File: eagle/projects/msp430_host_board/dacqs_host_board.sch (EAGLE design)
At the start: 107 parts, among them J1 MOL-SL-4-RA, J10 MOL-SL-3-V, J12 MOL-SL-2-V, J13 JST-PH-2TH-RA, J14 USB_MICROB_RECPT, J16 MOL-SL-2-RA, J17 CLM-112-02-L-D, J2 MOL-SL-4-RA, J3 MOL-SL-4-RA, J4 MOL-SL-4-RA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

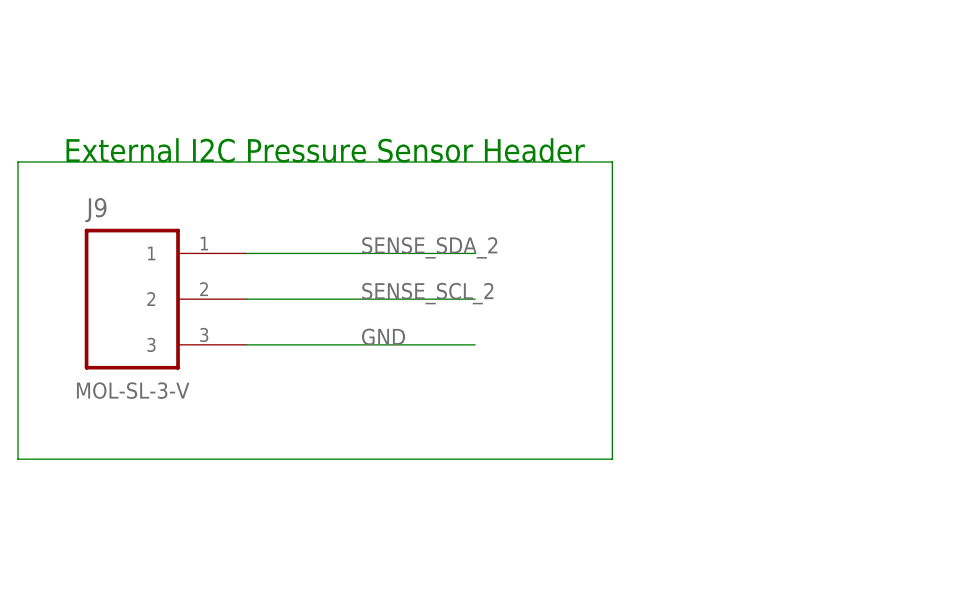
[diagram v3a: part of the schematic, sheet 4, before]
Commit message: Added power to balloon pressure sensor connector
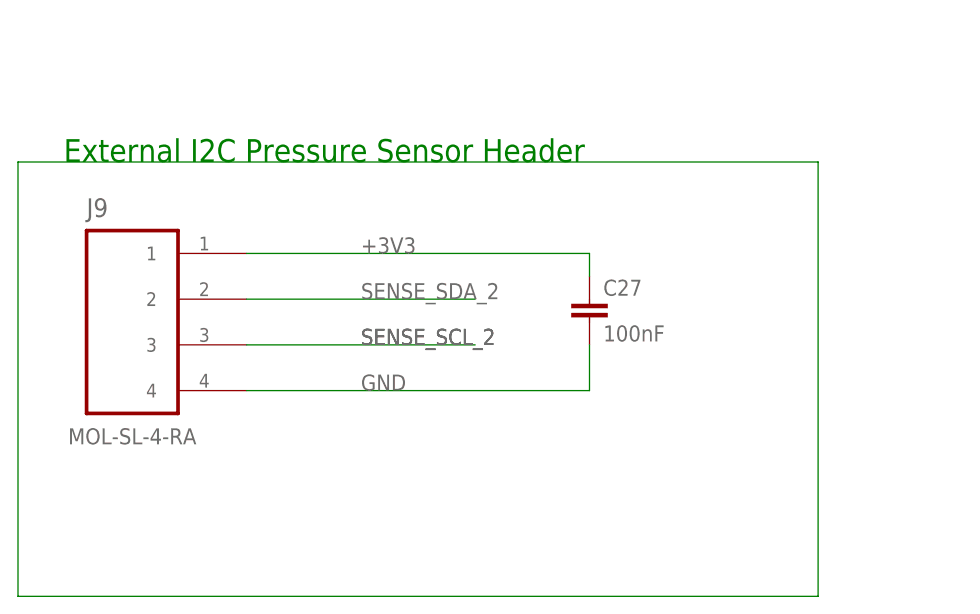
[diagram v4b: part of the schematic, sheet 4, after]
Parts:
- added C27: 100nF, daqcs_host:CAP_100NF0_0603
- J9: value MOL-SL-3-V -> MOL-SL-4-RA; device daqcs_host:MOLSL_3PIN_SL3V_V -> daqcs_host:MOLSL_4PIN_SL4RA_RA
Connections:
- net +3V3: now also C27.1, J9.1
- net GND: now also C27.2, J9.4; no longer J9.3
- net SENSE_SCL_2: now also J9.3; no longer J9.2
- net SENSE_SDA_2: now also J9.2; no longer J9.1
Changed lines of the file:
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@@
 <setting verticaltext="up"/>
 </settings>
-<grid distance="0.1" unitdist="inch" unit="inch" style="lines" multiple="1" display="yes" altdistance="0.01" altunitdist="inch" altunit="inch"/>
+<grid distance="0.1" unitdist="inch" unit="inch" style="lines" multiple="1" display="no" altdistance="0.01" altunitdist="inch" altunit="inch"/>
 <layers>
 <layer number="1" name="Top" color="4" fill="1" visible="no" active="no"/>
@@
 <part name="J7" library="daqcs_host" deviceset="MOLSL_5PIN" device="_V" technology="_SL4V" value="MOL-SL-5-V"/>
 <part name="J8" library="daqcs_host" deviceset="MOLSL_3PIN" device="_RA" technology="_SL3RA" value="MOL-SL-3-RA"/>
-<part name="J9" library="daqcs_host" deviceset="MOLSL_3PIN" device="_V" technology="_SL3V" value="MOL-SL-3-V"/>
 <part name="J10" library="daqcs_host" deviceset="MOLSL_3PIN" device="_V" technology="_SL3V" value="MOL-SL-3-V"/>
 <part name="H1" library="daqcs_host" deviceset="MOUNT-HOLE" device="_2.75"/>
@@
 <part name="SUPPLY36" library="supply2" deviceset="GND" device=""/>
 <part name="SUPPLY37" library="supply2" deviceset="GND" device=""/>
+<part name="J9" library="daqcs_host" deviceset="MOLSL_4PIN" device="_RA" technology="_SL4RA" value="MOL-SL-4-RA"/>
+<part name="C27" library="daqcs_host" deviceset="CAP" device="_0603" technology="_100NF0" value="100nF"/>
 </parts>
 <sheets>
@@
 <instance part="J7" gate="G$1" x="55.88" y="195.58"/>
 <instance part="J8" gate="G$1" x="55.88" y="134.62"/>
-<instance part="J9" gate="G$1" x="55.88" y="66.04"/>
 <instance part="J10" gate="G$1" x="218.44" y="127"/>
 <instance part="H1" gate="G$1" x="213.36" y="71.12"/>
@@
 <instance part="H3" gate="G$1" x="213.36" y="55.88"/>
 <instance part="H4" gate="G$1" x="256.54" y="55.88"/>
+<instance part="J9" gate="G$1" x="55.88" y="63.5"/>
+<instance part="C27" gate="G$1" x="106.68" y="63.5"/>
 </instances>
 <busses>
@@
 </segment>
 <segment>
-<wire x1="68.58" y1="60.96" x2="93.98" y2="60.96" width="0.1524" layer="91"/>
-<label x="81.28" y="60.96" size="1.778" layer="95"/>
-<pinref part="J9" gate="G$1" pin="3"/>
-</segment>
-<segment>
 <pinref part="SUPPLY10" gate="GND" pin="GND"/>
 <wire x1="195.58" y1="182.88" x2="195.58" y2="187.96" width="0.1524" layer="91"/>
@@
 <pinref part="J10" gate="G$1" pin="3"/>
 </segment>
+<segment>
+<pinref part="J9" gate="G$1" pin="4"/>
+<wire x1="68.58" y1="55.88" x2="106.68" y2="55.88" width="0.1524" layer="91"/>
+<label x="81.28" y="55.88" size="1.778" layer="95"/>
+<pinref part="C27" gate="G$1" pin="2"/>
+<wire x1="106.68" y1="60.96" x2="106.68" y2="55.88" width="0.1524" layer="91"/>
+</segment>
 </net>
 <net name="ACT_SPEED_IN" class="0">
@@
 <net name="SENSE_SDA_2" class="0">
 <segment>
-<wire x1="68.58" y1="71.12" x2="93.98" y2="71.12" width="0.1524" layer="91"/>
-<label x="81.28" y="71.12" size="1.778" layer="95"/>
-<pinref part="J9" gate="G$1" pin="1"/>
-</segment>
-</net>
-<net name="SENSE_SCL_2" class="0">
-<segment>
 <wire x1="68.58" y1="66.04" x2="93.98" y2="66.04" width="0.1524" layer="91"/>
 <label x="81.28" y="66.04" size="1.778" layer="95"/>
 <pinref part="J9" gate="G$1" pin="2"/>
+</segment>
+</net>
+<net name="SENSE_SCL_2" class="0">
+<segment>
+<wire x1="68.58" y1="60.96" x2="93.98" y2="60.96" width="0.1524" layer="91"/>
+<label x="81.28" y="60.96" size="1.778" layer="95"/>
+<pinref part="J9" gate="G$1" pin="3"/>
+<label x="81.28" y="60.96" size="1.778" layer="95"/>
 </segment>
 </net>
@@
 <wire x1="246.38" y1="203.2" x2="246.38" y2="208.28" width="0.1524" layer="91"/>
 </segment>
+<segment>
+<wire x1="68.58" y1="71.12" x2="106.68" y2="71.12" width="0.1524" layer="91"/>
+<label x="81.28" y="71.12" size="1.778" layer="95"/>
+<pinref part="J9" gate="G$1" pin="1"/>
+<pinref part="C27" gate="G$1" pin="1"/>
+<wire x1="106.68" y1="71.12" x2="106.68" y2="68.58" width="0.1524" layer="91"/>
+</segment>
 </net>
 <net name="SBWTCK_MOTOR" class="0">
@@
 <net name="N$18" class="0">
 <segment>
-<wire x1="43.18" y1="81.28" x2="109.22" y2="81.28" width="0.1524" layer="91"/>
-<wire x1="109.22" y1="81.28" x2="109.22" y2="48.26" width="0.1524" layer="91"/>
-<wire x1="109.22" y1="48.26" x2="43.18" y2="48.26" width="0.1524" layer="91"/>
-<wire x1="43.18" y1="48.26" x2="43.18" y2="81.28" width="0.1524" layer="91"/>
-</segment>
-</net>
+<wire x1="43.18" y1="81.28" x2="132.08" y2="81.28" width="0.1524" layer="91"/>
+<wire x1="132.08" y1="81.28" x2="132.08" y2="33.02" width="0.1524" layer="91"/>
+<wire x1="132.08" y1="33.02" x2="43.18" y2="33.02" width="0.1524" layer="91"/>
+<wire x1="43.18" y1="33.02" x2="43.18" y2="81.28" width="0.1524" layer="91"/>
+</segment>
+</net>

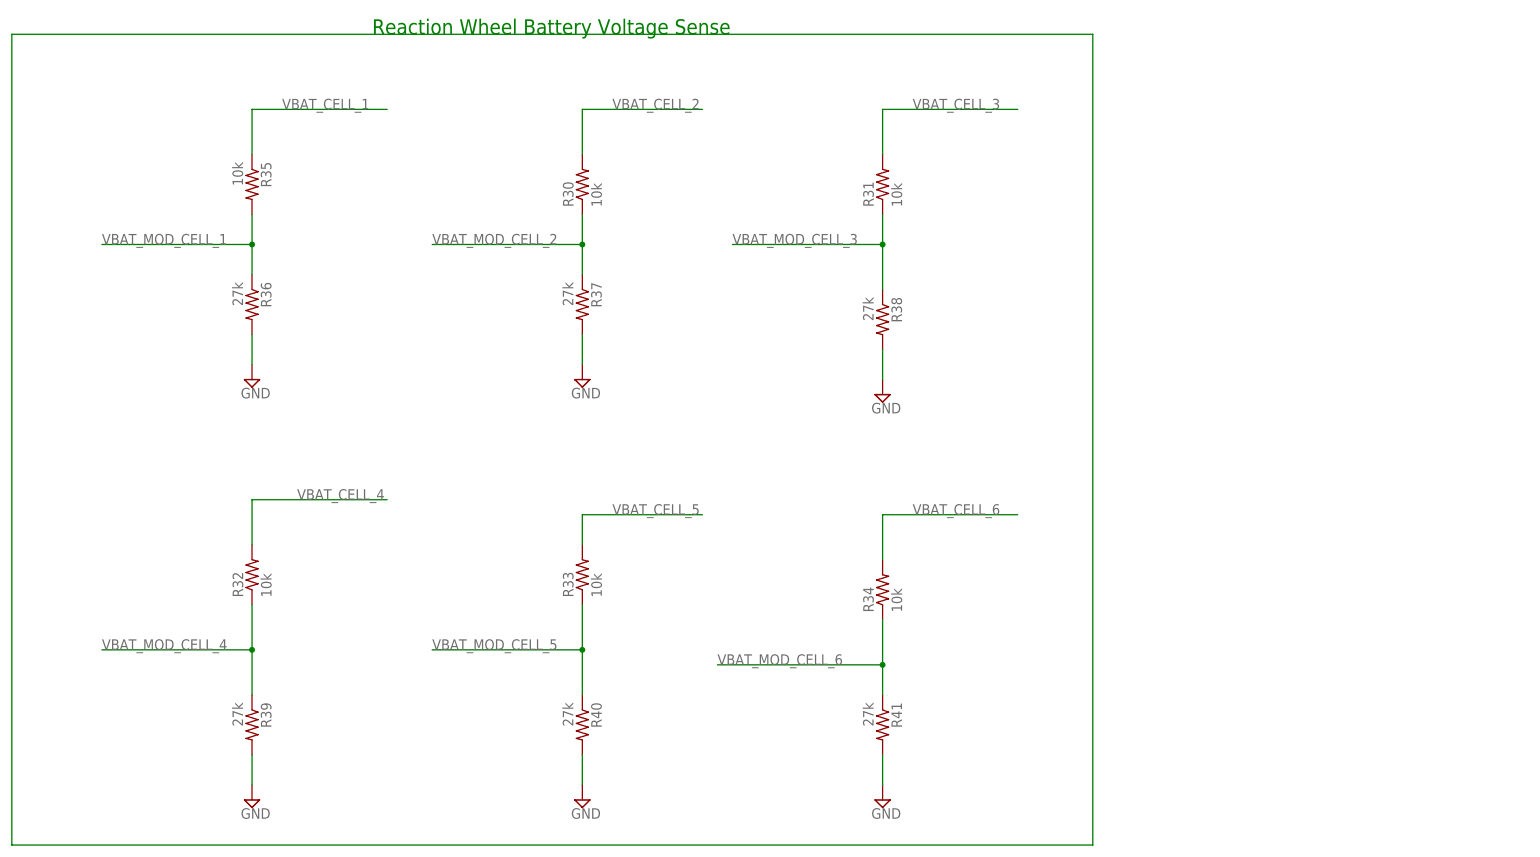
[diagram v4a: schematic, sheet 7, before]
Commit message: Added 7 pin SL connector for reaction wheel battery Vsense
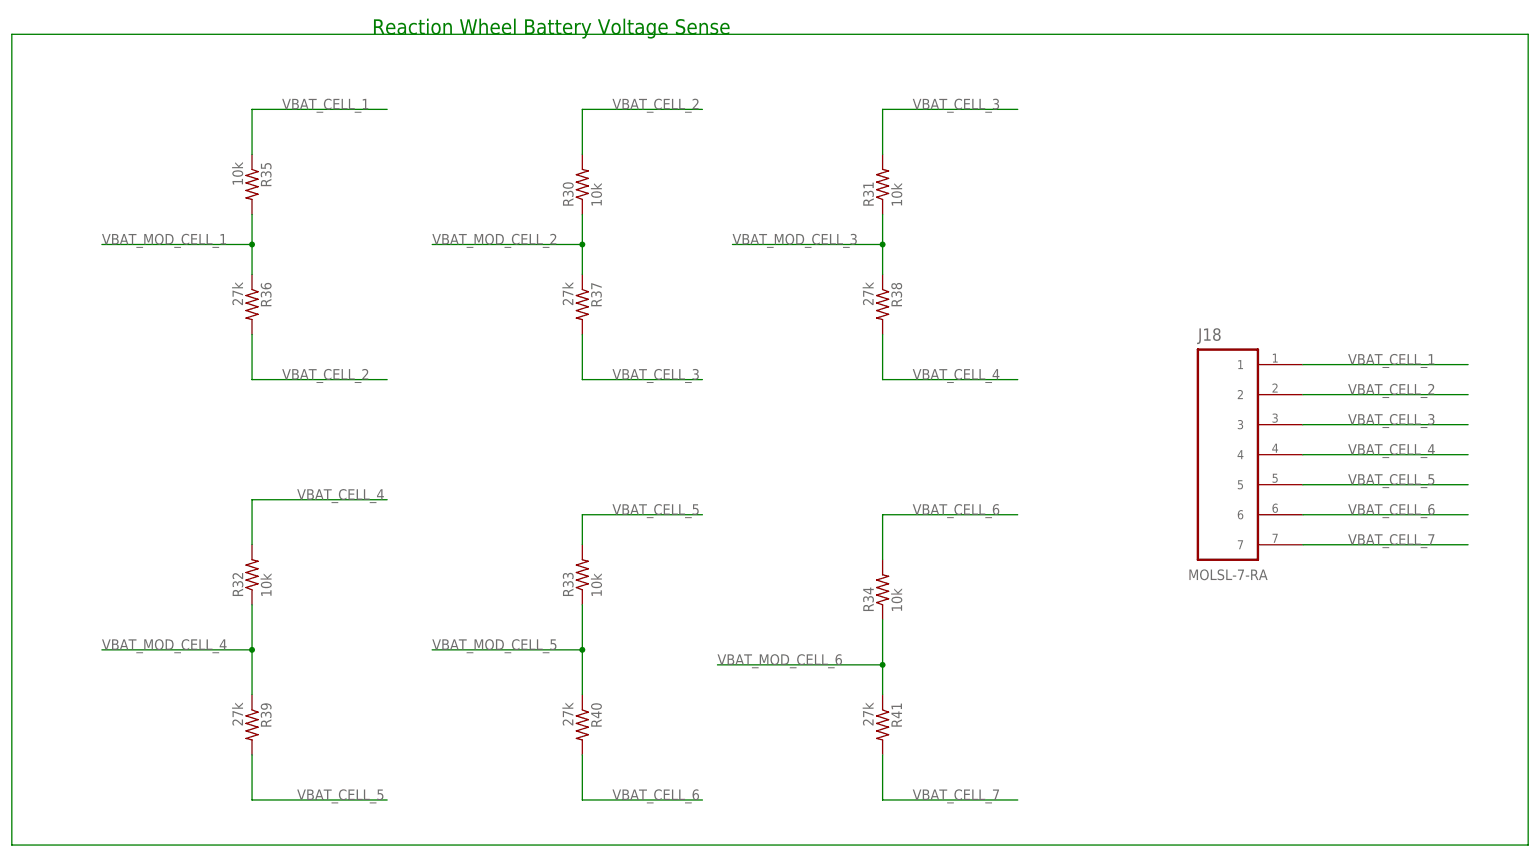
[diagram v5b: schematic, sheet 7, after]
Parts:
- added J18: MOLSL-7-RA, daqcs_host:MOLSL_7PIN_RA
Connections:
- new net VBAT_CELL_7: J18.7, R41.2
- net GND: no longer R36.2, R37.2, R38.2, R39.2, R40.2, R41.2
- net VBAT_CELL_1: now also J18.1
- net VBAT_CELL_2: now also J18.2, R36.2
- net VBAT_CELL_3: now also J18.3, R37.2
- net VBAT_CELL_4: now also J18.4, R38.2
- net VBAT_CELL_5: now also J18.5, R39.2
- net VBAT_CELL_6: now also J18.6, R40.2
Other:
- moved on the sheet: R38
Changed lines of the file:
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@@
 <setting verticaltext="up"/>
 </settings>
-<grid distance="0.1" unitdist="inch" unit="inch" style="lines" multiple="1" display="no" altdistance="0.01" altunitdist="inch" altunit="inch"/>
+<grid distance="0.1" unitdist="inch" unit="inch" style="lines" multiple="1" display="yes" altdistance="0.01" altunitdist="inch" altunit="inch"/>
 <layers>
 <layer number="1" name="Top" color="4" fill="1" visible="no" active="no"/>
@@
 <part name="R40" library="daqcs_host" deviceset="RES" device="_0603" technology="_27R0" value="27k"/>
 <part name="R41" library="daqcs_host" deviceset="RES" device="_0603" technology="_27R0" value="27k"/>
-<part name="SUPPLY31" library="supply2" deviceset="GND" device=""/>
-<part name="SUPPLY33" library="supply2" deviceset="GND" device=""/>
-<part name="SUPPLY34" library="supply2" deviceset="GND" device=""/>
-<part name="SUPPLY35" library="supply2" deviceset="GND" device=""/>
-<part name="SUPPLY36" library="supply2" deviceset="GND" device=""/>
-<part name="SUPPLY37" library="supply2" deviceset="GND" device=""/>
 <part name="J9" library="daqcs_host" deviceset="MOLSL_4PIN" device="_RA" technology="_SL4RA" value="MOL-SL-4-RA"/>
 <part name="C27" library="daqcs_host" deviceset="CAP" device="_0603" technology="_100NF0" value="100nF"/>
+<part name="J18" library="daqcs_host" deviceset="MOLSL_7PIN" device="_RA" value="MOLSL-7-RA"/>
 </parts>
 <sheets>
@@
 <instance part="R36" gate="G$1" x="76.2" y="167.64" rot="R270"/>
 <instance part="R37" gate="G$1" x="132.08" y="167.64" rot="R270"/>
-<instance part="R38" gate="G$1" x="182.88" y="165.1" rot="R270"/>
+<instance part="R38" gate="G$1" x="182.88" y="167.64" rot="R270"/>
 <instance part="R39" gate="G$1" x="76.2" y="96.52" rot="R270"/>
 <instance part="R40" gate="G$1" x="132.08" y="96.52" rot="R270"/>
 <instance part="R41" gate="G$1" x="182.88" y="96.52" rot="R270"/>
-<instance part="SUPPLY31" gate="GND" x="76.2" y="154.94"/>
-<instance part="SUPPLY33" gate="GND" x="132.08" y="154.94"/>
-<instance part="SUPPLY34" gate="GND" x="182.88" y="152.4"/>
-<instance part="SUPPLY35" gate="GND" x="182.88" y="83.82"/>
-<instance part="SUPPLY36" gate="GND" x="132.08" y="83.82"/>
-<instance part="SUPPLY37" gate="GND" x="76.2" y="83.82"/>
+<instance part="J18" gate="G$1" x="241.3" y="142.24"/>
 </instances>
 <busses>
@@
 <wire x1="76.2" y1="200.66" x2="99.06" y2="200.66" width="0.1524" layer="91"/>
 <label x="81.28" y="200.66" size="1.778" layer="95"/>
+</segment>
+<segment>
+<pinref part="J18" gate="G$1" pin="1"/>
+<wire x1="254" y1="157.48" x2="281.94" y2="157.48" width="0.1524" layer="91"/>
+<label x="261.62" y="157.48" size="1.778" layer="95"/>
 </segment>
 </net>
@@
 <label x="137.16" y="200.66" size="1.778" layer="95"/>
 </segment>
+<segment>
+<pinref part="J18" gate="G$1" pin="2"/>
+<wire x1="254" y1="152.4" x2="281.94" y2="152.4" width="0.1524" layer="91"/>
+<label x="261.62" y="152.4" size="1.778" layer="95"/>
+</segment>
+<segment>
+<pinref part="R36" gate="G$1" pin="2"/>
+<wire x1="76.2" y1="162.56" x2="76.2" y2="154.94" width="0.1524" layer="91"/>
+<wire x1="76.2" y1="154.94" x2="99.06" y2="154.94" width="0.1524" layer="91"/>
+<label x="81.28" y="154.94" size="1.778" layer="95"/>
+</segment>
 </net>
 <net name="VBAT_MOD_CELL_2" class="0">
@@
 <pinref part="R38" gate="G$1" pin="1"/>
 <wire x1="182.88" y1="182.88" x2="182.88" y2="177.8" width="0.1524" layer="91"/>
-<wire x1="182.88" y1="177.8" x2="182.88" y2="170.18" width="0.1524" layer="91"/>
+<wire x1="182.88" y1="177.8" x2="182.88" y2="172.72" width="0.1524" layer="91"/>
 <wire x1="182.88" y1="177.8" x2="157.48" y2="177.8" width="0.1524" layer="91"/>
 <junction x="182.88" y="177.8"/>
@@
 <label x="187.96" y="200.66" size="1.778" layer="95"/>
 </segment>
+<segment>
+<pinref part="J18" gate="G$1" pin="3"/>
+<wire x1="254" y1="147.32" x2="281.94" y2="147.32" width="0.1524" layer="91"/>
+<label x="261.62" y="147.32" size="1.778" layer="95"/>
+</segment>
+<segment>
+<pinref part="R37" gate="G$1" pin="2"/>
+<wire x1="132.08" y1="162.56" x2="132.08" y2="154.94" width="0.1524" layer="91"/>
+<wire x1="132.08" y1="154.94" x2="152.4" y2="154.94" width="0.1524" layer="91"/>
+<label x="137.16" y="154.94" size="1.778" layer="95"/>
+</segment>
 </net>
 <net name="VBAT_CELL_4" class="0">
@@
 <wire x1="76.2" y1="134.62" x2="99.06" y2="134.62" width="0.1524" layer="91"/>
 <label x="83.82" y="134.62" size="1.778" layer="95"/>
+</segment>
+<segment>
+<pinref part="J18" gate="G$1" pin="4"/>
+<wire x1="254" y1="142.24" x2="281.94" y2="142.24" width="0.1524" layer="91"/>
+<label x="261.62" y="142.24" size="1.778" layer="95"/>
+</segment>
+<segment>
+<pinref part="R38" gate="G$1" pin="2"/>
+<wire x1="182.88" y1="162.56" x2="182.88" y2="154.94" width="0.1524" layer="91"/>
+<wire x1="182.88" y1="154.94" x2="205.74" y2="154.94" width="0.1524" layer="91"/>
+<label x="187.96" y="154.94" size="1.778" layer="95"/>
 </segment>
 </net>
@@
 <label x="137.16" y="132.08" size="1.778" layer="95"/>
 </segment>
+<segment>
+<pinref part="J18" gate="G$1" pin="5"/>
+<wire x1="254" y1="137.16" x2="281.94" y2="137.16" width="0.1524" layer="91"/>
+<label x="261.62" y="137.16" size="1.778" layer="95"/>
+</segment>
+<segment>
+<pinref part="R39" gate="G$1" pin="2"/>
+<wire x1="76.2" y1="91.44" x2="76.2" y2="83.82" width="0.1524" layer="91"/>
+<wire x1="76.2" y1="83.82" x2="99.06" y2="83.82" width="0.1524" layer="91"/>
+<label x="83.82" y="83.82" size="1.778" layer="95"/>
+</segment>
 </net>
 <net name="VBAT_MOD_CELL_5" class="0">
@@
 <label x="187.96" y="132.08" size="1.778" layer="95"/>
 </segment>
+<segment>
+<pinref part="J18" gate="G$1" pin="6"/>
+<wire x1="254" y1="132.08" x2="281.94" y2="132.08" width="0.1524" layer="91"/>
+<label x="261.62" y="132.08" size="1.778" layer="95"/>
+</segment>
+<segment>
+<pinref part="R40" gate="G$1" pin="2"/>
+<wire x1="132.08" y1="91.44" x2="132.08" y2="83.82" width="0.1524" layer="91"/>
+<wire x1="132.08" y1="83.82" x2="152.4" y2="83.82" width="0.1524" layer="91"/>
+<label x="137.16" y="83.82" size="1.778" layer="95"/>
+</segment>
 </net>
 <net name="VBAT_MOD_CELL_6" class="0">
@@
 </segment>
 </net>
-<net name="GND" class="0">
-<segment>
-<pinref part="R36" gate="G$1" pin="2"/>
-<wire x1="76.2" y1="162.56" x2="76.2" y2="157.48" width="0.1524" layer="91"/>
-<pinref part="SUPPLY31" gate="GND" pin="GND"/>
-</segment>
-<segment>
-<pinref part="R37" gate="G$1" pin="2"/>
-<wire x1="132.08" y1="162.56" x2="132.08" y2="157.48" width="0.1524" layer="91"/>
-<pinref part="SUPPLY33" gate="GND" pin="GND"/>
-</segment>
-<segment>
-<pinref part="R38" gate="G$1" pin="2"/>
-<wire x1="182.88" y1="160.02" x2="182.88" y2="154.94" width="0.1524" layer="91"/>
-<pinref part="SUPPLY34" gate="GND" pin="GND"/>
+<net name="N$56" class="0">
+<segment>
+<wire x1="35.56" y1="213.36" x2="292.1" y2="213.36" width="0.1524" layer="91"/>
+<wire x1="292.1" y1="213.36" x2="292.1" y2="76.2" width="0.1524" layer="91"/>
+<wire x1="292.1" y1="76.2" x2="35.56" y2="76.2" width="0.1524" layer="91"/>
+<wire x1="35.56" y1="76.2" x2="35.56" y2="213.36" width="0.1524" layer="91"/>
+</segment>
+</net>
+<net name="VBAT_CELL_7" class="0">
+<segment>
+<pinref part="J18" gate="G$1" pin="7"/>
+<wire x1="254" y1="127" x2="281.94" y2="127" width="0.1524" layer="91"/>
+<label x="261.62" y="127" size="1.778" layer="95"/>
 </segment>
 <segment>
 <pinref part="R41" gate="G$1" pin="2"/>
-<wire x1="182.88" y1="91.44" x2="182.88" y2="86.36" width="0.1524" layer="91"/>
-<pinref part="SUPPLY35" gate="GND" pin="GND"/>
-</segment>
-<segment>
-<pinref part="R40" gate="G$1" pin="2"/>
-<wire x1="132.08" y1="91.44" x2="132.08" y2="86.36" width="0.1524" layer="91"/>
-<pinref part="SUPPLY36" gate="GND" pin="GND"/>
-</segment>
-<segment>
-<pinref part="R39" gate="G$1" pin="2"/>
-<wire x1="76.2" y1="91.44" x2="76.2" y2="86.36" width="0.1524" layer="91"/>
-<pinref part="SUPPLY37" gate="GND" pin="GND"/>
-</segment>
-</net>
-<net name="N$56" class="0">
-<segment>
-<wire x1="35.56" y1="213.36" x2="218.44" y2="213.36" width="0.1524" layer="91"/>
-<wire x1="218.44" y1="213.36" x2="218.44" y2="76.2" width="0.1524" layer="91"/>
-<wire x1="218.44" y1="76.2" x2="35.56" y2="76.2" width="0.1524" layer="91"/>
-<wire x1="35.56" y1="76.2" x2="35.56" y2="213.36" width="0.1524" layer="91"/>
-</segment>
-</net>
+<wire x1="182.88" y1="91.44" x2="182.88" y2="83.82" width="0.1524" layer="91"/>
+<wire x1="182.88" y1="83.82" x2="205.74" y2="83.82" width="0.1524" layer="91"/>
+<label x="187.96" y="83.82" size="1.778" layer="95"/>
+</segment>
+</net>
